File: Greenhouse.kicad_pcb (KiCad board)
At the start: 2 copper layers, 143.8 x 46.8 mm, 28 parts, among them J1 Conn_01x03, J2 Conn_02x20_Odd_Even, U2 IS31FL3197, U2 LTV-847S

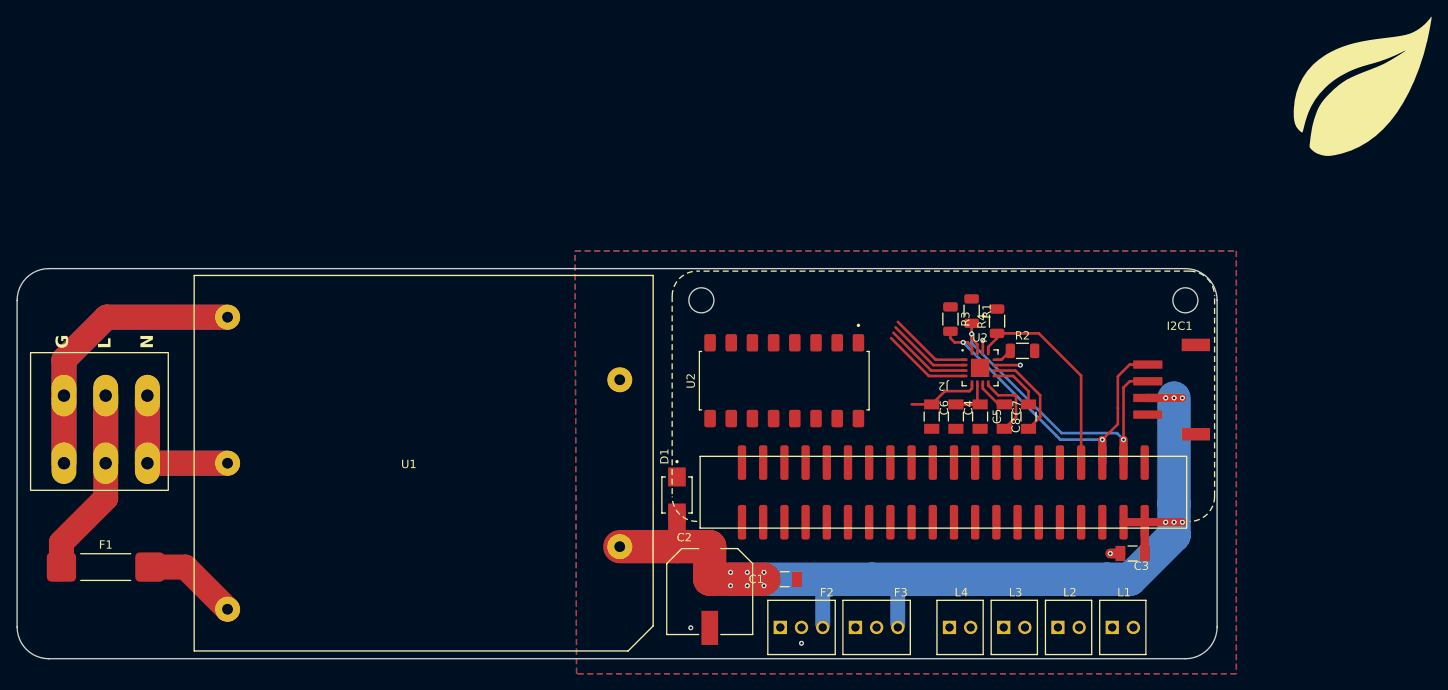
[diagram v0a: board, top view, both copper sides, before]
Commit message: updated schematic & pcb with latest part selections
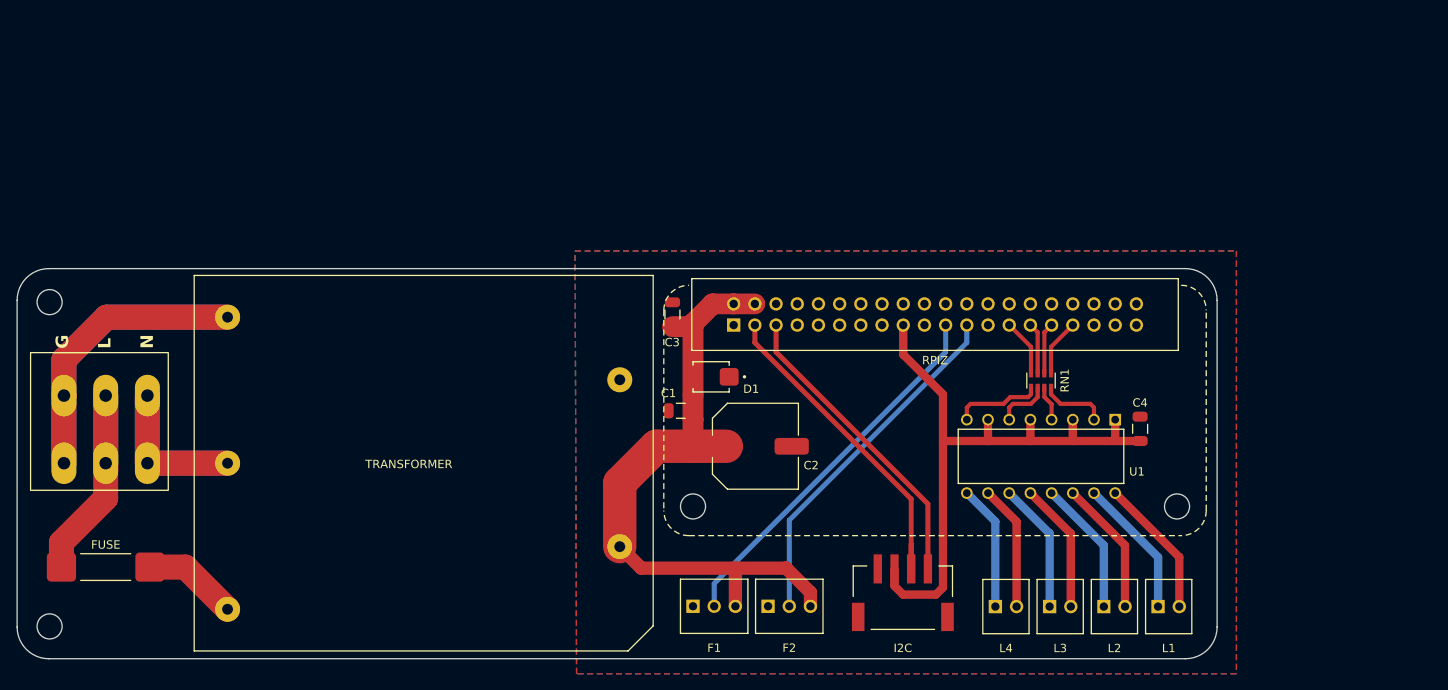
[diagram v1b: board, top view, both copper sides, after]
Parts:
- removed C5, C6, C7, C8: C, Greenhouse-Footprints:CAPC3216X180N
- removed F3: Conn_01x03, Greenhouse-Footprints:TE_282834-3
- removed the G*** at (198.2, 38.6)
- removed I2C1: Conn_01x04, Greenhouse-Footprints:JST_S4B-PH-SM4-TB
- removed J2: Conn_02x20_Odd_Even, Greenhouse-Footprints:Raspi Zero W Socket SMD
- removed R1, R2, R3, R4: R_US, Resistor_SMD:R_1206_3216Metric
- removed U2: LTV-847S, Greenhouse-Footprints:SOIC254P1016X460-16N
- removed U2: IS31FL3197, Greenhouse-Footprints:QFN-16_EP_4x4_Pitch0.65mm
- added F1: Conn_01x03, Greenhouse-Footprints:TE_282834-3, F.Cu at (120.5, 101.0)
- added I2C: Conn_01x04, Greenhouse-Footprints:JST_S4B-PH-SM4-TB, F.Cu at (143.1, 96.5)
- added REF**: mounting hole, Greenhouse-Footprints:mounting hole, F.Cu at (40.9, 103.4)
- added REF**: mounting hole, Greenhouse-Footprints:mounting hole, F.Cu at (40.9, 64.5)
- added RN1: CAY16-271J4LF, Greenhouse-Footprints:RESCAF80P320X160X60-8N, F.Cu at (159.7, 73.9)
- added RPIZ: Conn_02x20_Odd_Even, Greenhouse-Footprints:Raspi Zero W Socket TH, F.Cu at (147.0, 66.0)
- added U1: LTV-847S, Greenhouse-Footprints:DIP880W50P254L2034H450Q16, F.Cu at (159.7, 83.0)
- C1: value C -> 1µF
- C2: value C_Polarized -> 330µF
- C3, C4: value C -> .1µF
- moved C3 62.1 mm to (115.5, 66.0), turned to 90 degrees
- moved C1 23.7 mm to (116.5, 77.5), turned to 180 degrees
- moved C4 22.1 mm to (171.6, 79.7), turned to 90 degrees
- moved C2 18.3 mm to (125.5, 81.8), turned to 0 degrees
- moved D1 14.7 mm to (120.2, 73.5), turned to 180 degrees
- moved L1 6.04 mm to (175.0, 101.0)
- moved L2 6.04 mm to (168.5, 101.0)
- moved L3 6.04 mm to (162.0, 101.0)
- moved L4 6.04 mm to (155.5, 101.0)
- moved F2 2.93 mm to (129.5, 101.0)
- renumbered F1 to FUSE, U1 to TRANSFORMER
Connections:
- F2 pad 2: PWM1 -> GPIO14
- J1 pad 2: NEUT -> LINE
- J1 pad 3: LINE -> NEUT
- TRANSFORMER pad 5: (no net) -> GND
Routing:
- net +3V3: track 5.30 -> 75.9 mm
- net (no net): track 66.3 -> 0.00 mm
- net GPIO13: track 0.00 -> 45.2 mm
- net GPIO14: track 0.00 -> 42.5 mm
- net +5V: track 118.9 -> 79.2 mm, vias 12 -> 0
- net NEUT: track 0.00 -> 35.4 mm
- net LINE: track 0.00 -> 30.8 mm
- net GPIO7: track 25.3 -> 0.00 mm
- net Net-(L1-Pin_1): track 0.00 -> 16.8 mm
- net Net-(L1-Pin_2): track 0.00 -> 16.8 mm
- net Net-(L2-Pin_2): track 0.00 -> 16.2 mm
- net Net-(L2-Pin_1): track 0.00 -> 16.2 mm
- net Net-(L3-Pin_2): track 0.00 -> 15.6 mm
- net Net-(L3-Pin_1): track 0.00 -> 15.6 mm
- net Net-(L4-Pin_2): track 0.00 -> 15.0 mm
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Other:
- rule pad_to_mask_clearance: 0 -> 0.05

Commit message: Finalized PCB layout, updated/added footprint models
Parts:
- removed L1, L2, L3, L4: Conn_01x02_Socket, Greenhouse-Footprints:TE_282834-2
- removed the REF** at (40.9, 103.4)
- removed the REF** at (40.9, 64.5)
- added J2: 282834-8, Greenhouse-Footprints:TE_282834-8, F.Cu at (167.0, 101.2)
- added REF**: mounting hole, Greenhouse-Footprints:mounting hole, F.Cu at (40.8, 103.5)
- added REF**: mounting hole, Greenhouse-Footprints:mounting hole, F.Cu at (40.8, 64.3)
- F1, F2: footprint Greenhouse-Footprints:TE_282834-3 -> Greenhouse-Footprints:Fan Header 3,4-pin through hole right angle
- moved I2C 21.3 mm to (121.8, 97.2)
- moved F2 20.7 mm to (148.7, 93.2), turned to 180 degrees
- moved F1 17.2 mm to (135.9, 93.2), turned to 180 degrees
- moved D1 7.83 mm to (117.6, 80.9), turned to 90 degrees
- moved C3 6.59 mm to (117.7, 72.2), turned to 0 degrees
- moved C2 3.39 mm to (126.9, 78.7)
- moved C1 2.75 mm to (117.7, 75.0), turned to 0 degrees
- moved C5 2.19 mm to (173.2, 78.2)
- moved U1 1.97 mm to (161.0, 81.5)
- moved RN1 1.00 mm to (159.7, 72.9)
- renumbered C4 to C5
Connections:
- F1 pad 1: GND -> PWM1
- F1 pad 2: GPIO13 -> GPIO2
- F2 pad 1: GND -> PWM0
- F2 pad 2: GPIO14 -> GPIO3
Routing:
- net PWM0: track 0.00 -> 69.2 mm
- net PWM1: track 0.00 -> 65.5 mm
- net GPIO13: track 45.2 -> 0.00 mm
- net GPIO14: track 42.5 -> 0.00 mm
- net GPIO3: track 0.00 -> 33.6 mm
- net GPIO2: track 0.00 -> 24.8 mm
- net SDA1: track 40.3 -> 31.4 mm, vias 0 -> 1
- net +5V: track 79.2 -> 87.7 mm
- net +3V3: track 75.9 -> 82.3 mm, vias 0 -> 3
- net SCL1: track 36.8 -> 31.2 mm, vias 0 -> 1
- net Net-(J2-Pad1): track 15.0 -> 17.7 mm
- net Net-(J2-Pad2): track 15.0 -> 17.7 mm
- net Net-(RN1-Pad6): track 6.49 -> 4.20 mm
- net Net-(RN1-Pad5): track 10.6 -> 8.28 mm
- net Net-(J2-Pad3): track 15.6 -> 17.7 mm
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
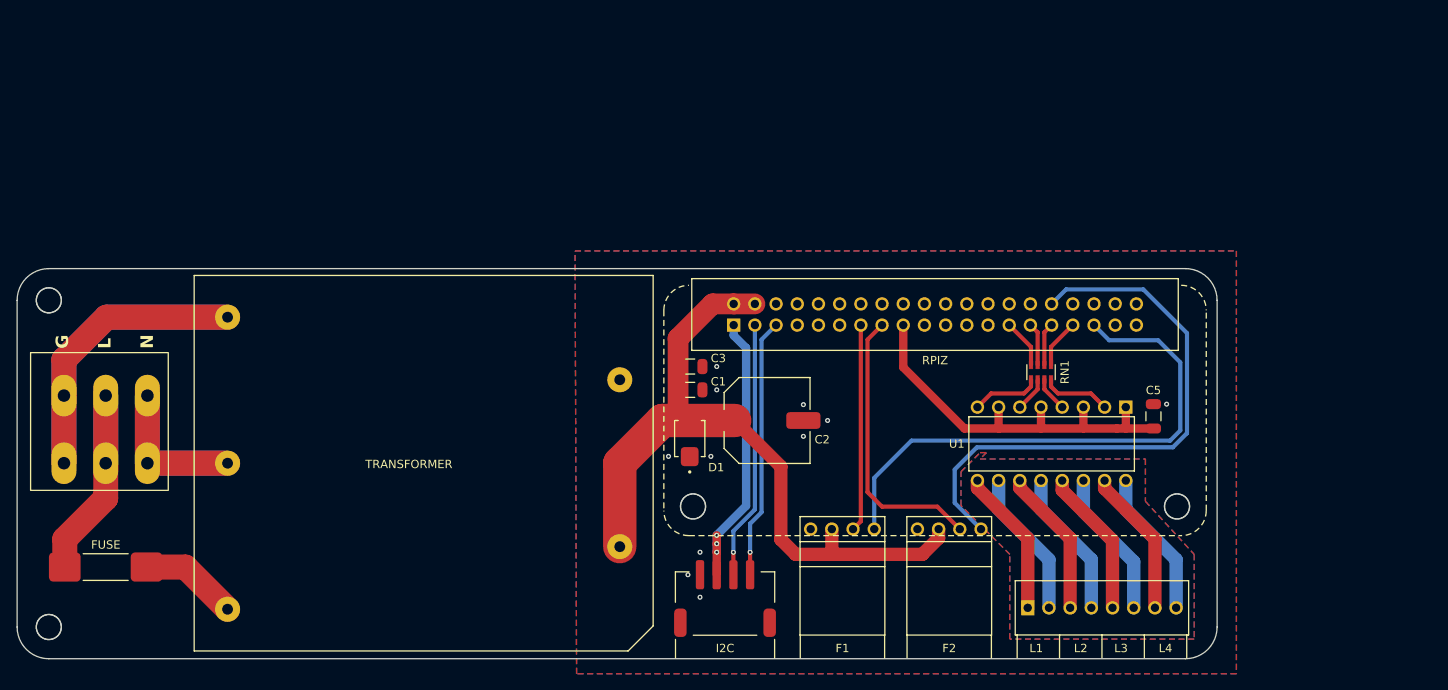
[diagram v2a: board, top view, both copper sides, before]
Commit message: Added customized footprints for the three edge headers to include guide marks, fixed bug with GPIO net labels
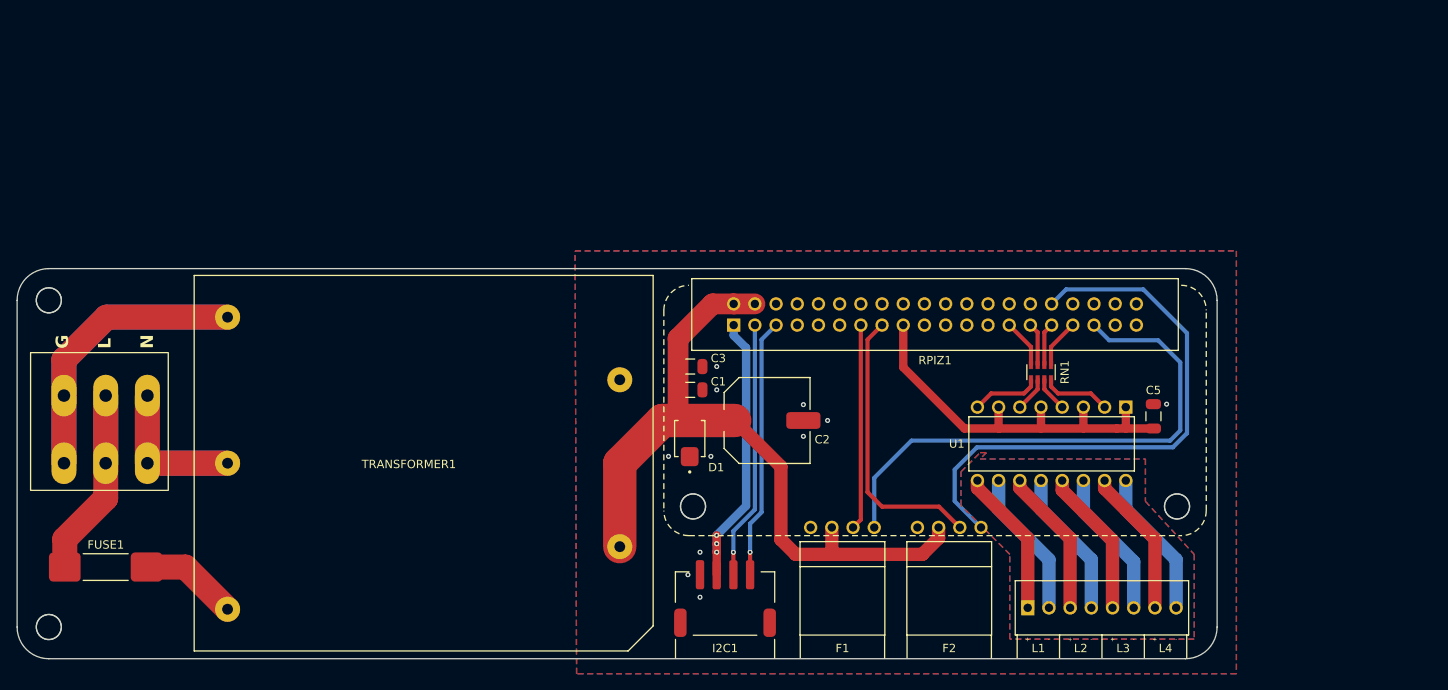
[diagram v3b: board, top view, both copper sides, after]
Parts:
- F1, F2: footprint Greenhouse-Footprints:Fan Header 3,4-pin through hole right angle -> Greenhouse-Footprints:Fan Header 3,4-pin through hole right angle, custom
- I2C1: renamed from I2C; footprint Greenhouse-Footprints:JST_S4B-PH-SM4-TB -> Greenhouse-Footprints:JST_S4B-PH-SM4-TB, custom
- J2: footprint Greenhouse-Footprints:TE_282834-8 -> Greenhouse-Footprints:TE_282834-8, custom
- renumbered FUSE to FUSE1, RPIZ to RPIZ1, TRANSFORMER to TRANSFORMER1
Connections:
- net GPIO28 renamed GPIO20
- F1 pad 2: GPIO2 -> GPIO27
- F2 pad 2: GPIO3 -> GPIO22
- RN1 pad 1: GPIO23 -> GPIO13
- RN1 pad 2: GPIO22 -> GPIO6
- RN1 pad 3: GPIO21 -> GPIO5
- RN1 pad 4: GPIO30 -> GPIO0
- RPIZ1 pad 10: GPIO16 -> GPIO15
- RPIZ1 pad 11: GPIO0 -> GPIO17
- RPIZ1 pad 12: GPIO1 -> GPIO18
- RPIZ1 pad 13: GPIO2 -> GPIO27
- RPIZ1 pad 15: GPIO3 -> GPIO22
- RPIZ1 pad 16: GPIO4 -> GPIO23
- RPIZ1 pad 18: GPIO5 -> GPIO24
- RPIZ1 pad 19: GPIO12 -> GPIO10
- RPIZ1 pad 21: GPIO13 -> GPIO9
- RPIZ1 pad 22: GPIO6 -> GPIO25
- RPIZ1 pad 23: GPIO14 -> GPIO11
- RPIZ1 pad 24: GPIO10 -> GPIO8
- RPIZ1 pad 26: GPIO11 -> GPIO7
- RPIZ1 pad 27: GPIO30 -> GPIO0
- RPIZ1 pad 28: GPIO31 -> GPIO1
- RPIZ1 pad 29: GPIO21 -> GPIO5
- RPIZ1 pad 31: GPIO22 -> GPIO6
- RPIZ1 pad 33: GPIO23 -> GPIO13
- RPIZ1 pad 36: GPIO27 -> GPIO16
- RPIZ1 pad 37: GPIO25 -> GPIO26
- RPIZ1 pad 40: GPIO29 -> GPIO21
- RPIZ1 pad 7: GPIO7 -> GPIO4
- RPIZ1 pad 8: GPIO15 -> GPIO14
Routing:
- net GPIO3: track 33.6 -> 0.00 mm
- net GPIO22: track 5.13 -> 33.6 mm
- net GPIO2: track 24.8 -> 0.00 mm
- net GPIO27: track 0.00 -> 24.6 mm
- net GPIO30: track 5.85 -> 0.00 mm
- net GPIO0: track 0.00 -> 5.85 mm
- net GPIO23: track 5.85 -> 0.00 mm
- net GPIO13: track 0.00 -> 5.85 mm
- net GPIO6: track 0.00 -> 5.13 mm
- net GPIO5: track 0.00 -> 5.13 mm
- net GPIO21: track 5.13 -> 0.00 mm

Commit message: Final PCB adjustments from footprint changes and added stitching vias
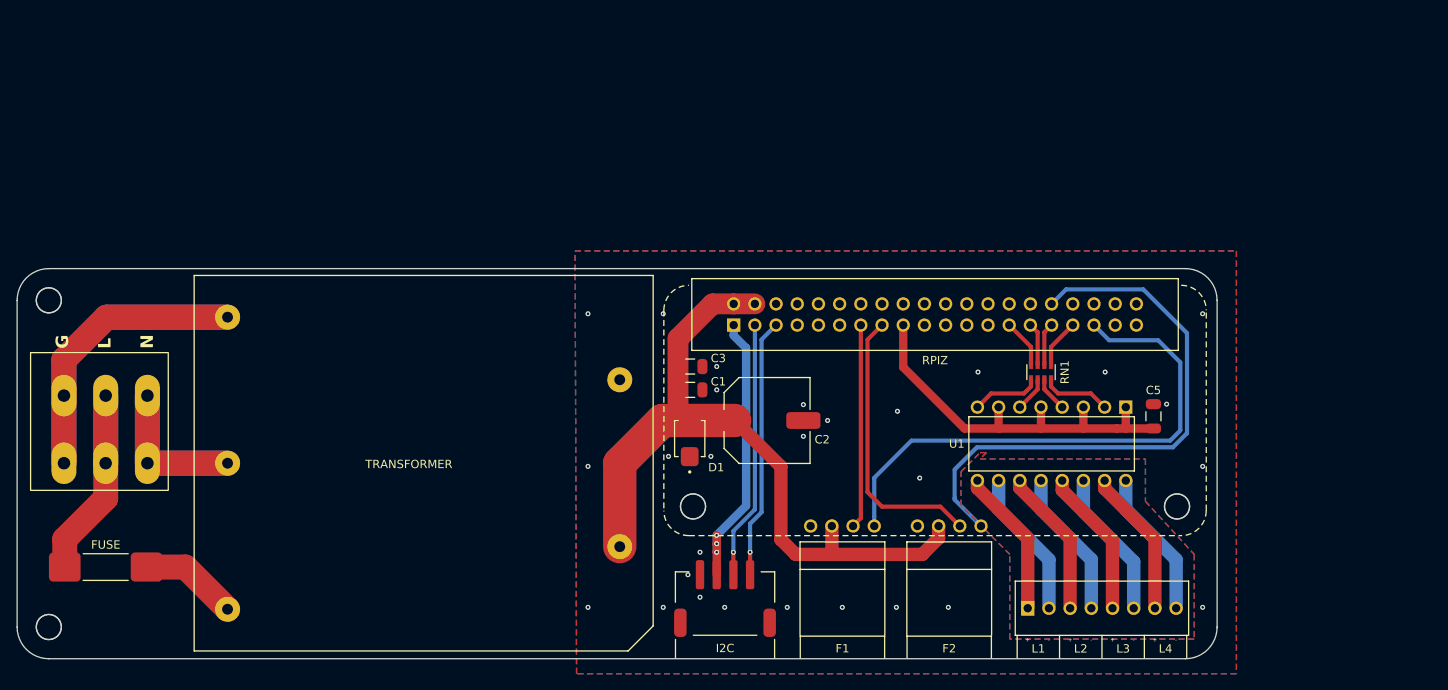
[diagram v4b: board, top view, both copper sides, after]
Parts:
- renumbered FUSE1 to FUSE, I2C1 to I2C, RPIZ1 to RPIZ, TRANSFORMER1 to TRANSFORMER
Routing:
- net GND: vias 11 -> 28
